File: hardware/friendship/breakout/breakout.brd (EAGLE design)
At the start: 91 x 29.5 mm, 7 parts, among them IC1 MAX481CSA, IC2 MAX481CSA

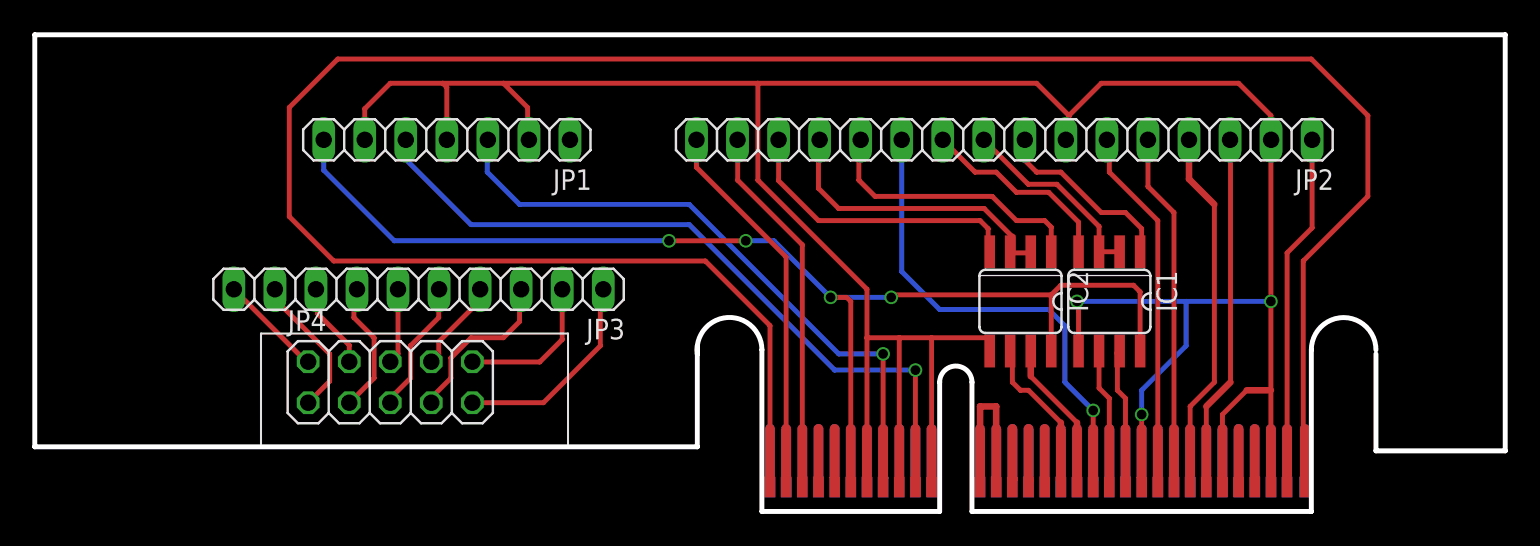
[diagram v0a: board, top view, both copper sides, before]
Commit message: moved busmaster plug
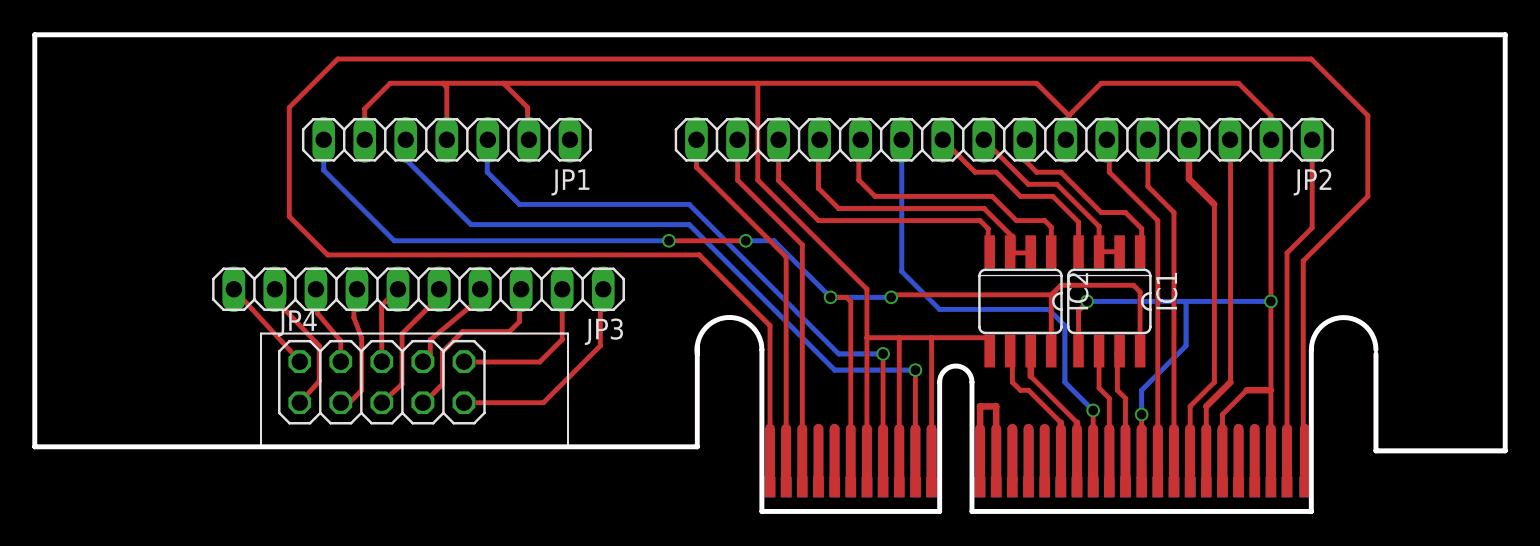
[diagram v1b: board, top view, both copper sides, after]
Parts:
- moved JP4 0.52 mm to (21.5, 8.00)
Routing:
- net N$29: track 10.5 -> 11.3 mm
- net N$32: track 13.2 -> 13.7 mm
- net N$31: track 9.25 -> 9.77 mm
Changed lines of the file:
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@@
 <setting verticaltext="up"/>
 </settings>
-<grid distance="0.25" unitdist="mm" unit="mm" style="lines" multiple="1" display="no" altdistance="0.025" altunitdist="inch" altunit="inch"/>
+<grid distance="0.125" unitdist="mm" unit="mm" style="lines" multiple="1" display="no" altdistance="0.025" altunitdist="inch" altunit="inch"/>
 <layers>
 <layer number="1" name="Top" color="4" fill="1" visible="yes" active="yes"/>
@@
 <element name="JP2" library="pinhead" package="1X16" value="" x="60" y="23" rot="R180"/>
 <element name="JP3" library="pinhead" package="1X10" value="" x="23.75" y="13.75" rot="R180"/>
-<element name="JP4" library="pinhead" package="2X05" value="" x="22" y="8"/>
+<element name="JP4" library="pinhead" package="2X05" value="" x="21.48" y="8"/>
 </elements>
 <signals>
@@
 <wire x1="18.75" y1="28" x2="15.75" y2="25" width="0.3048" layer="1"/>
 <wire x1="15.75" y1="25" x2="15.75" y2="18.25" width="0.3048" layer="1"/>
-<wire x1="15.75" y1="18.25" x2="18.5" y2="15.5" width="0.3048" layer="1"/>
-<wire x1="18.5" y1="15.5" x2="41.5" y2="15.5" width="0.3048" layer="1"/>
-<wire x1="41.5" y1="15.5" x2="45.5" y2="11.5" width="0.3048" layer="1"/>
+<wire x1="15.75" y1="18.25" x2="18.125" y2="15.875" width="0.3048" layer="1"/>
+<wire x1="18.125" y1="15.875" x2="41.125" y2="15.875" width="0.3048" layer="1"/>
+<wire x1="41.125" y1="15.875" x2="45.5" y2="11.5" width="0.3048" layer="1"/>
 <wire x1="45.5" y1="11.5" x2="45.5" y2="1.5" width="0.3048" layer="1"/>
 <wire x1="45.5" y1="1.5" x2="45.5" y2="1.51" width="0" layer="19" extent="1-1"/>
@@
 <wire x1="76.5" y1="23.01" x2="76.51" y2="23" width="0.4064" layer="1"/>
 <via x="76.5" y="13" extent="1-16" drill="0.6"/>
-<wire x1="64.5" y1="13" x2="71.25" y2="13" width="0.3048" layer="16"/>
+<wire x1="65.125" y1="13" x2="71.25" y2="13" width="0.3048" layer="16"/>
 <wire x1="71.25" y1="13" x2="76.5" y2="13" width="0.3048" layer="16"/>
 <wire x1="76.5" y1="13" x2="76.5" y2="22.99" width="0.3048" layer="1"/>
@@
 <wire x1="71.25" y1="10.25" x2="71.25" y2="13" width="0.3048" layer="16"/>
 <wire x1="64.595" y1="9.9266" x2="64.595" y2="12.405" width="0.3048" layer="1"/>
-<wire x1="64.595" y1="12.405" x2="64.5" y2="13" width="0.3048" layer="1"/>
-<via x="64.5" y="13" extent="1-16" drill="0.6"/>
+<wire x1="64.595" y1="12.405" x2="65.125" y2="13" width="0.3048" layer="1"/>
+<via x="65.125" y="13" extent="1-16" drill="0.6"/>
 <wire x1="51.5" y1="1.51" x2="51.5" y2="10.75" width="0.3048" layer="1"/>
 <contactref element="U$1" pad="A09(GND)"/>
@@
 <contactref element="JP2" pad="10"/>
 <wire x1="64.595" y1="16.0734" x2="64.595" y2="17.905" width="0.3048" layer="1"/>
-<wire x1="64.595" y1="17.905" x2="62.75" y2="19.75" width="0.3048" layer="1"/>
-<wire x1="62.75" y1="19.75" x2="60.75" y2="19.75" width="0.3048" layer="1"/>
-<wire x1="60.75" y1="19.75" x2="59.5" y2="21" width="0.3048" layer="1"/>
+<wire x1="64.595" y1="17.905" x2="63" y2="19.5" width="0.3048" layer="1"/>
+<wire x1="63" y1="19.5" x2="61" y2="19.5" width="0.3048" layer="1"/>
+<wire x1="61" y1="19.5" x2="59.5" y2="21" width="0.3048" layer="1"/>
 <wire x1="59.5" y1="21" x2="58.19" y2="21" width="0.3048" layer="1"/>
 <wire x1="58.19" y1="21" x2="56.19" y2="23" width="0.3048" layer="1"/>
@@
 <contactref element="JP4" pad="2"/>
 <contactref element="JP3" pad="10"/>
-<wire x1="16.92" y1="9.27" x2="16.8" y2="9.27" width="0.3048" layer="1"/>
-<wire x1="16.8" y1="9.27" x2="12.32" y2="13.75" width="0.3048" layer="1"/>
+<wire x1="16.4" y1="9.27" x2="16.425" y2="9.27" width="0.3048" layer="1"/>
+<wire x1="16.425" y1="9.27" x2="12.32" y2="13.75" width="0.3048" layer="1"/>
 </signal>
 <signal name="N$24">
@@
 <contactref element="JP4" pad="1"/>
 <wire x1="14.86" y1="13.75" x2="14.86" y2="13.14" width="0.3048" layer="1"/>
-<wire x1="14.86" y1="13.14" x2="18.25" y2="9.75" width="0.3048" layer="1"/>
-<wire x1="18.25" y1="9.75" x2="18.25" y2="8.06" width="0.3048" layer="1"/>
-<wire x1="18.25" y1="8.06" x2="16.92" y2="6.73" width="0.3048" layer="1"/>
+<wire x1="14.86" y1="13.14" x2="17.605" y2="10.25" width="0.3048" layer="1"/>
+<wire x1="17.605" y1="10.25" x2="17.605" y2="8.06" width="0.3048" layer="1"/>
+<wire x1="17.605" y1="8.06" x2="16.4" y2="6.73" width="0.3048" layer="1"/>
 </signal>
 <signal name="N$25">
 <contactref element="JP3" pad="8"/>
 <contactref element="JP4" pad="4"/>
-<wire x1="19.46" y1="9.27" x2="19.46" y2="10.29" width="0.3048" layer="1"/>
-<wire x1="19.46" y1="10.29" x2="17.5" y2="12.25" width="0.3048" layer="1"/>
+<wire x1="18.94" y1="9.27" x2="18.94" y2="10.54" width="0.3048" layer="1"/>
+<wire x1="18.94" y1="10.54" x2="17.5" y2="12.25" width="0.3048" layer="1"/>
 <wire x1="17.5" y1="12.25" x2="17.5" y2="13.65" width="0.3048" layer="1"/>
 <wire x1="17.5" y1="13.65" x2="17.4" y2="13.75" width="0.3048" layer="1"/>
@@
 <contactref element="JP3" pad="7"/>
 <contactref element="JP4" pad="3"/>
-<wire x1="19.46" y1="6.73" x2="19.48" y2="6.73" width="0.3048" layer="1"/>
-<wire x1="19.48" y1="6.73" x2="21" y2="8.25" width="0.3048" layer="1"/>
-<wire x1="21" y1="8.25" x2="21" y2="10.75" width="0.3048" layer="1"/>
-<wire x1="21" y1="10.75" x2="19.75" y2="12" width="0.3048" layer="1"/>
+<wire x1="18.94" y1="6.73" x2="19.48" y2="6.73" width="0.3048" layer="1"/>
+<wire x1="19.48" y1="6.73" x2="20.23" y2="7.5" width="0.3048" layer="1"/>
+<wire x1="20.23" y1="7.5" x2="20.23" y2="10.75" width="0.3048" layer="1"/>
+<wire x1="20.23" y1="10.75" x2="19.75" y2="12" width="0.3048" layer="1"/>
 <wire x1="19.75" y1="12" x2="19.75" y2="13.56" width="0.3048" layer="1"/>
 <wire x1="19.75" y1="13.56" x2="19.94" y2="13.75" width="0.3048" layer="1"/>
@@
 <contactref element="JP3" pad="6"/>
 <contactref element="JP4" pad="6"/>
-<wire x1="22.48" y1="13.75" x2="22.48" y2="9.75" width="0.3048" layer="1"/>
-<wire x1="22.48" y1="9.75" x2="22" y2="9.27" width="0.3048" layer="1"/>
+<wire x1="22.48" y1="13.75" x2="21.46" y2="12.75" width="0.3048" layer="1"/>
+<wire x1="21.46" y1="12.75" x2="21.48" y2="9.27" width="0.3048" layer="1"/>
 </signal>
 <signal name="N$28">
 <contactref element="JP3" pad="5"/>
 <contactref element="JP4" pad="5"/>
-<wire x1="22" y1="6.73" x2="22" y2="7" width="0.3048" layer="1"/>
-<wire x1="22" y1="7" x2="23.25" y2="8.25" width="0.3048" layer="1"/>
-<wire x1="23.25" y1="8.25" x2="23.25" y2="10.25" width="0.3048" layer="1"/>
-<wire x1="23.25" y1="10.25" x2="25" y2="12" width="0.3048" layer="1"/>
-<wire x1="25" y1="12" x2="25" y2="13.73" width="0.3048" layer="1"/>
+<wire x1="21.48" y1="6.73" x2="21.5" y2="6.75" width="0.3048" layer="1"/>
+<wire x1="21.5" y1="6.75" x2="22.73" y2="7.875" width="0.3048" layer="1"/>
+<wire x1="22.73" y1="7.875" x2="22.73" y2="11" width="0.3048" layer="1"/>
+<wire x1="22.73" y1="11" x2="25" y2="13.25" width="0.3048" layer="1"/>
+<wire x1="25" y1="13.25" x2="25" y2="13.73" width="0.3048" layer="1"/>
 <wire x1="25" y1="13.73" x2="25.02" y2="13.75" width="0.3048" layer="1"/>
 </signal>
@@
 <contactref element="JP4" pad="7"/>
 <contactref element="JP3" pad="3"/>
-<wire x1="24.54" y1="6.73" x2="24.54" y2="7.04" width="0.3048" layer="1"/>
-<wire x1="24.54" y1="7.04" x2="25.75" y2="8.25" width="0.3048" layer="1"/>
-<wire x1="25.75" y1="8.25" x2="25.75" y2="9.5" width="0.3048" layer="1"/>
-<wire x1="25.75" y1="9.5" x2="27" y2="10.75" width="0.3048" layer="1"/>
-<wire x1="27" y1="10.75" x2="29" y2="10.75" width="0.3048" layer="1"/>
-<wire x1="29" y1="10.75" x2="30" y2="11.75" width="0.3048" layer="1"/>
+<wire x1="24.02" y1="6.73" x2="24.165" y2="6.79" width="0.3048" layer="1"/>
+<wire x1="24.165" y1="6.79" x2="25.23" y2="7.875" width="0.3048" layer="1"/>
+<wire x1="25.23" y1="7.875" x2="25.23" y2="9.875" width="0.3048" layer="1"/>
+<wire x1="25.23" y1="9.875" x2="26.48" y2="11.125" width="0.3048" layer="1"/>
+<wire x1="26.48" y1="11.125" x2="29.375" y2="11.125" width="0.3048" layer="1"/>
+<wire x1="29.375" y1="11.125" x2="30" y2="11.75" width="0.3048" layer="1"/>
 <wire x1="30" y1="11.75" x2="30" y2="13.65" width="0.3048" layer="1"/>
 <wire x1="30" y1="13.65" x2="30.1" y2="13.75" width="0.3048" layer="1"/>
@@
 <contactref element="JP3" pad="4"/>
 <contactref element="JP4" pad="8"/>
-<wire x1="27.56" y1="13.75" x2="27.56" y2="13.06" width="0.3048" layer="1"/>
-<wire x1="27.56" y1="13.06" x2="25" y2="10.5" width="0.3048" layer="1"/>
-<wire x1="25" y1="10.5" x2="25" y2="9.73" width="0.3048" layer="1"/>
-<wire x1="25" y1="9.73" x2="24.54" y2="9.27" width="0.3048" layer="1"/>
+<wire x1="27.56" y1="13.75" x2="27.56" y2="13.185" width="0.3048" layer="1"/>
+<wire x1="27.56" y1="13.185" x2="24.48" y2="10.625" width="0.3048" layer="1"/>
+<wire x1="24.48" y1="10.625" x2="24.48" y2="9.73" width="0.3048" layer="1"/>
+<wire x1="24.48" y1="9.73" x2="24.02" y2="9.27" width="0.3048" layer="1"/>
 </signal>
 <signal name="N$31">
@@
 <wire x1="32.64" y1="10.64" x2="31.25" y2="9.25" width="0.3048" layer="1"/>
 <wire x1="31.25" y1="9.25" x2="27.1" y2="9.25" width="0.3048" layer="1"/>
-<wire x1="27.1" y1="9.25" x2="27.08" y2="9.27" width="0.3048" layer="1"/>
+<wire x1="27.1" y1="9.25" x2="26.56" y2="9.27" width="0.3048" layer="1"/>
 </signal>
 <signal name="N$32">
 <contactref element="JP3" pad="1"/>
 <contactref element="JP4" pad="9"/>
-<wire x1="27.08" y1="6.73" x2="31.48" y2="6.73" width="0.3048" layer="1"/>
+<wire x1="26.56" y1="6.73" x2="31.48" y2="6.73" width="0.3048" layer="1"/>
 <wire x1="31.48" y1="6.73" x2="35" y2="10.25" width="0.3048" layer="1"/>
 <wire x1="35" y1="10.25" x2="35" y2="13.5" width="0.3048" layer="1"/>

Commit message: placed busmaster plug better on the breakout. fixes issue.
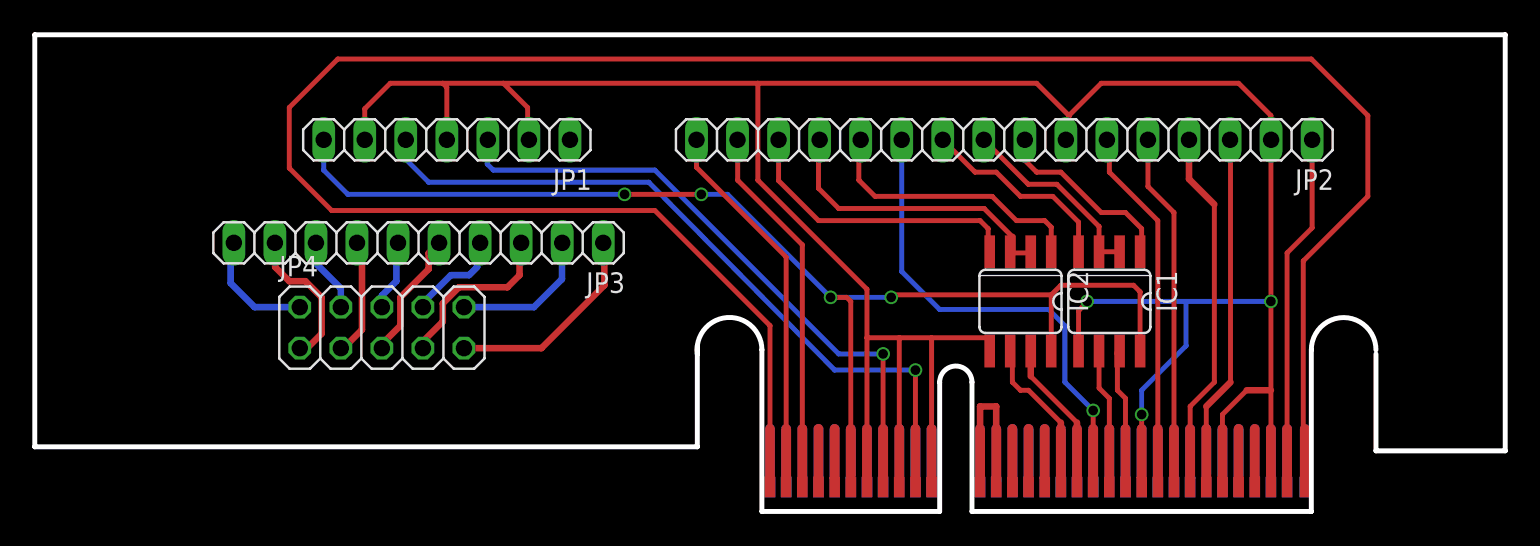
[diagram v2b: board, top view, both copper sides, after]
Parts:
- moved JP4 3.38 mm to (21.5, 11.4)
- moved JP3 2.88 mm to (23.8, 16.6)
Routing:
- net N$1: track 143.5 -> 141.7 mm
- net N$22: track 6.10 -> 7.47 mm
- net N$26: track 8.03 -> 7.29 mm
- net N$31: track 9.77 -> 9.04 mm
- net N$32: track 13.7 -> 13.0 mm
- net N$24: track 8.58 -> 9.13 mm
- net N$28: track 8.52 -> 7.99 mm
- net N$27: track 4.91 -> 4.39 mm
